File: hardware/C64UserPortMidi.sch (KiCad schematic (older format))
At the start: 15 parts, among them J1 C64-UserPort, J2 MIDI IN DIN-5, J3 AVR-ISP-6, U1 ATtiny13A-PU, U2 6N138, U3 74HC595

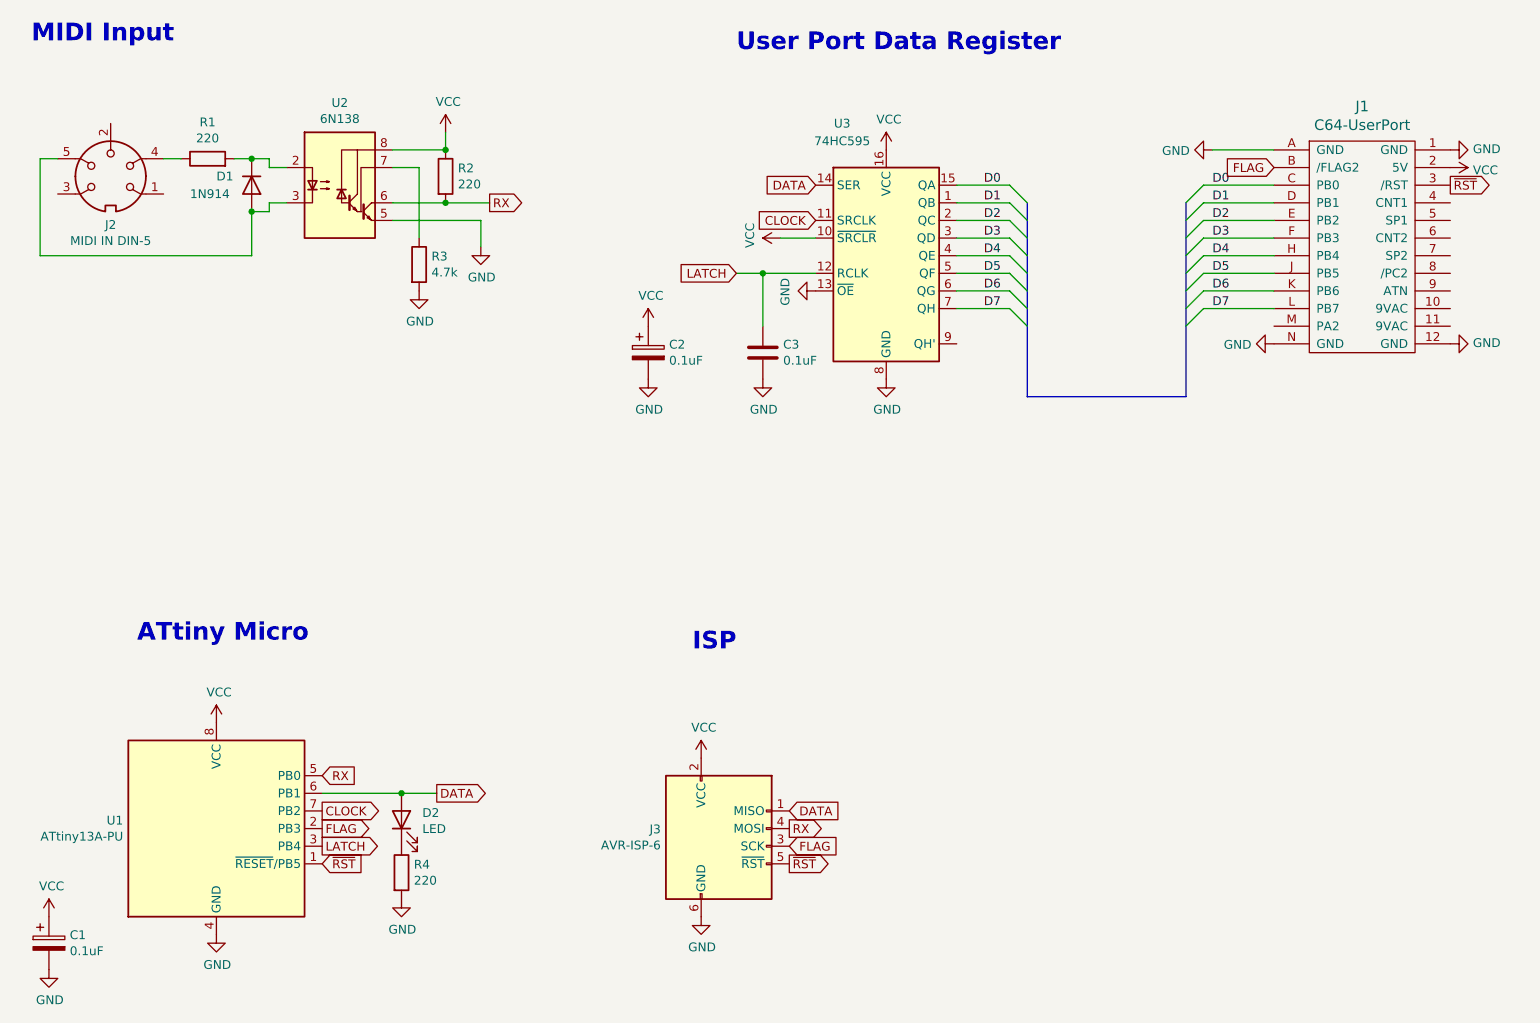
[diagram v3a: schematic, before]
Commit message: Alterations to hardware to allow better handshaking between c64 and attiny. Flag code removed in favor of combined latch. Improved delay routines. Swapped flag test to transfer test for maximum speed.
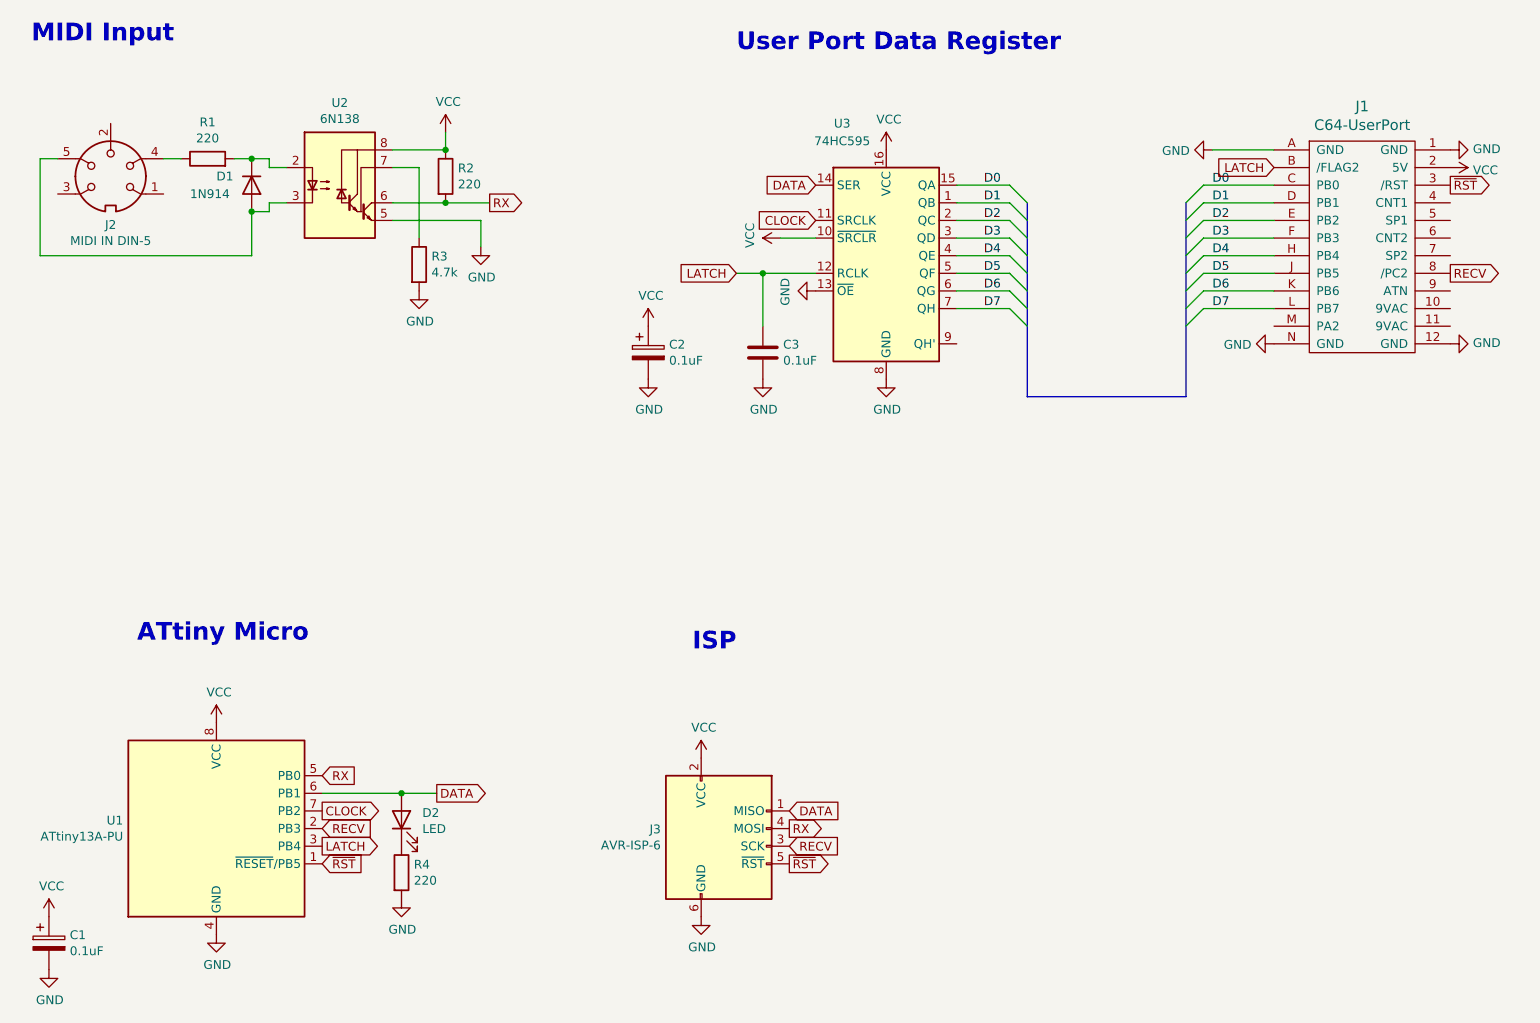
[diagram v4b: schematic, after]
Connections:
- net LATCH: now also J1.B (/FLAG2)
- net RECV: now reaches J1.8 (/PC2)
- net RECV: now also J3.3 (SCK), U1.2 (PB3)
- removed net FLAG: J1.B (/FLAG2), J3.3 (SCK), U1.2 (PB3)
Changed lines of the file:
@@
 	1    0    0    -1
 $EndComp
-Text GLabel 8500 2200 0    50   Input ~ 0
-FLAG
 Entry Wire Line
 	7000 2300 7100 2400
@@
 Text GLabel 5750 5850 2    50   Input ~ 0
 DATA
-Text GLabel 5750 6050 2    50   Input ~ 0
-FLAG
 $Comp
 L power:VCC #PWR0116
@@
 Wire Wire Line
 	5700 2600 5900 2600
-Text GLabel 3100 5950 2    50   Output ~ 0
-FLAG
 Text GLabel 3100 6050 2    50   Output ~ 0
 LATCH
@@
 	1    0    0    -1
 $EndComp
+Text GLabel 9500 2800 2    50   Output ~ 0
+RECV
+Text GLabel 3100 5950 2    50   Input ~ 0
+RECV
+Text GLabel 8500 2200 0    50   Input ~ 0
+LATCH
+Text GLabel 5750 6050 2    50   Input ~ 0
+RECV
 Wire Bus Line
 	8000 2400 8000 3500
